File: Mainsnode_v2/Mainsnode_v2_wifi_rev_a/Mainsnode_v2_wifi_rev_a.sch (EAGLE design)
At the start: 49 parts, among them J2 WIRE_HOLE-14AWG, J3 WIRE_HOLE-14AWG, J4 HOLE, J5 HOLE, J6 HOLE, J7 HOLE, K1 S216S01F, Q3 MMBT2222A

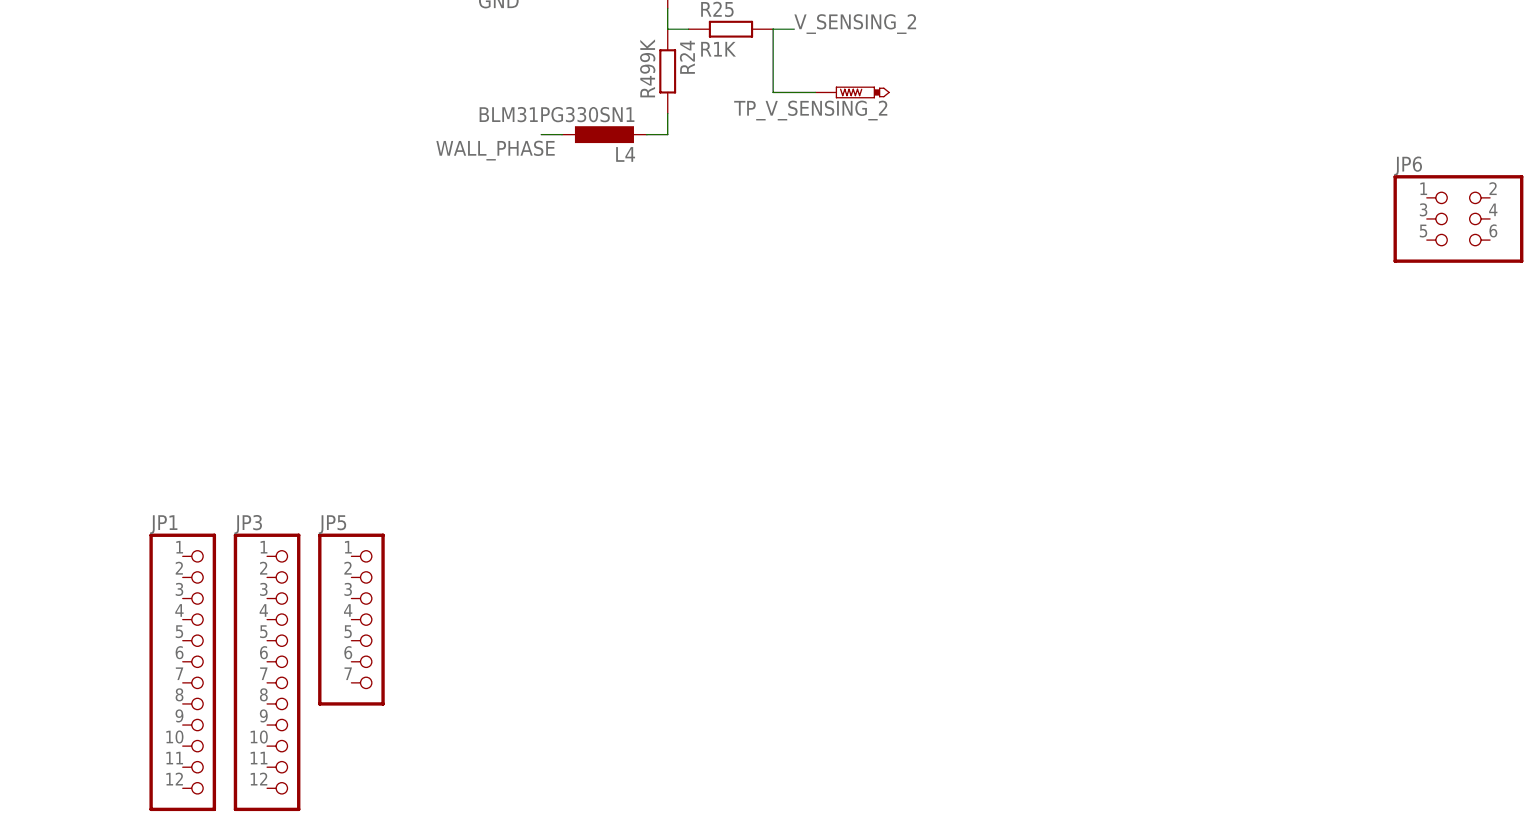
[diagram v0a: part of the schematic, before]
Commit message: updt wifi brd rev a (rmv cmpnents)
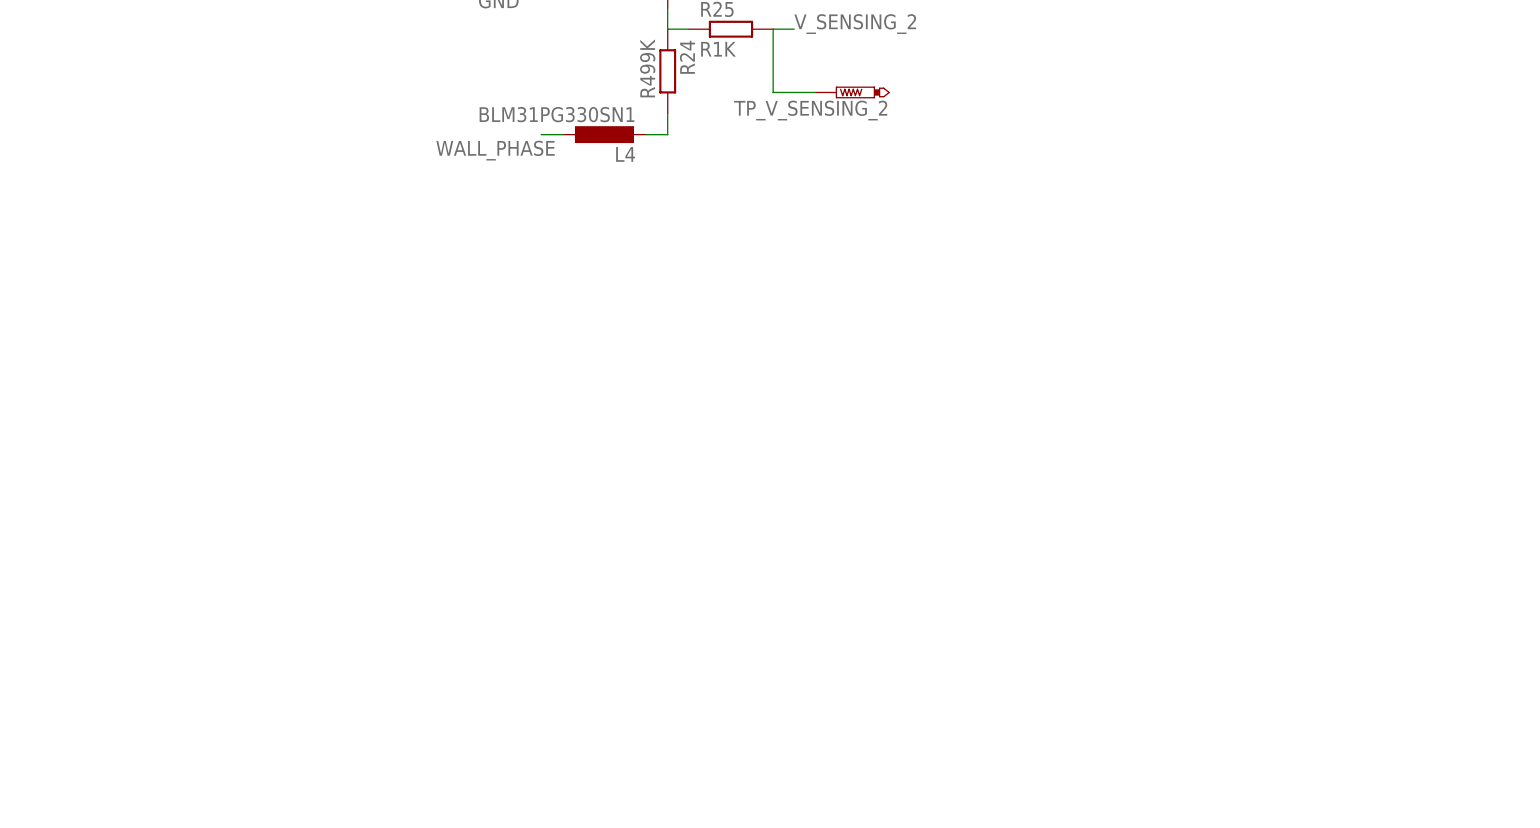
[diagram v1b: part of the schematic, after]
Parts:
- removed JP1, JP3: (no value), pinhead:PINHD-1X12
- removed JP5: (no value), pinhead:PINHD-1X7
- removed JP6: (no value), pinhead:PINHD-2X3
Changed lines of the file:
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@@
 <attribute name="TP_SIGNAL_NAME" value=""/>
 </part>
-<part name="JP1" library="pinhead" deviceset="PINHD-1X12" device=""/>
-<part name="JP3" library="pinhead" deviceset="PINHD-1X12" device=""/>
-<part name="JP5" library="pinhead" deviceset="PINHD-1X7" device=""/>
 <part name="R1" library="resistor-power" deviceset="R" device="KH206-8" value="R0.22W5"/>
 <part name="TP_GND" library="testpad" deviceset="PTR1" device="PAD1-13">
 <attribute name="TP_SIGNAL_NAME" value=""/>
 </part>
-<part name="JP6" library="pinhead" deviceset="PINHD-2X3" device=""/>
 </parts>
 <sheets>
@@
 <instance part="TP_V_SENSING_2" gate="G$1" x="312.42" y="132.08" rot="R90"/>
 <instance part="TP_I_SENSING" gate="G$1" x="330.2" y="200.66" rot="R270"/>
-<instance part="JP1" gate="G$1" x="236.22" y="63.5"/>
-<instance part="JP3" gate="G$1" x="246.38" y="63.5"/>
-<instance part="JP5" gate="A" x="256.54" y="68.58"/>
 <instance part="R1" gate="G$1" x="368.3" y="200.66" rot="R270"/>
 <instance part="TP_GND" gate="G$1" x="335.28" y="157.48" rot="R90"/>
-<instance part="JP6" gate="A" x="386.08" y="116.84"/>
 </instances>
 <busses>
